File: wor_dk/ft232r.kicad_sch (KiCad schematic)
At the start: 22 parts, among them J401 USB_C_Receptacle_USB2.0_16P, U401 FT232RL

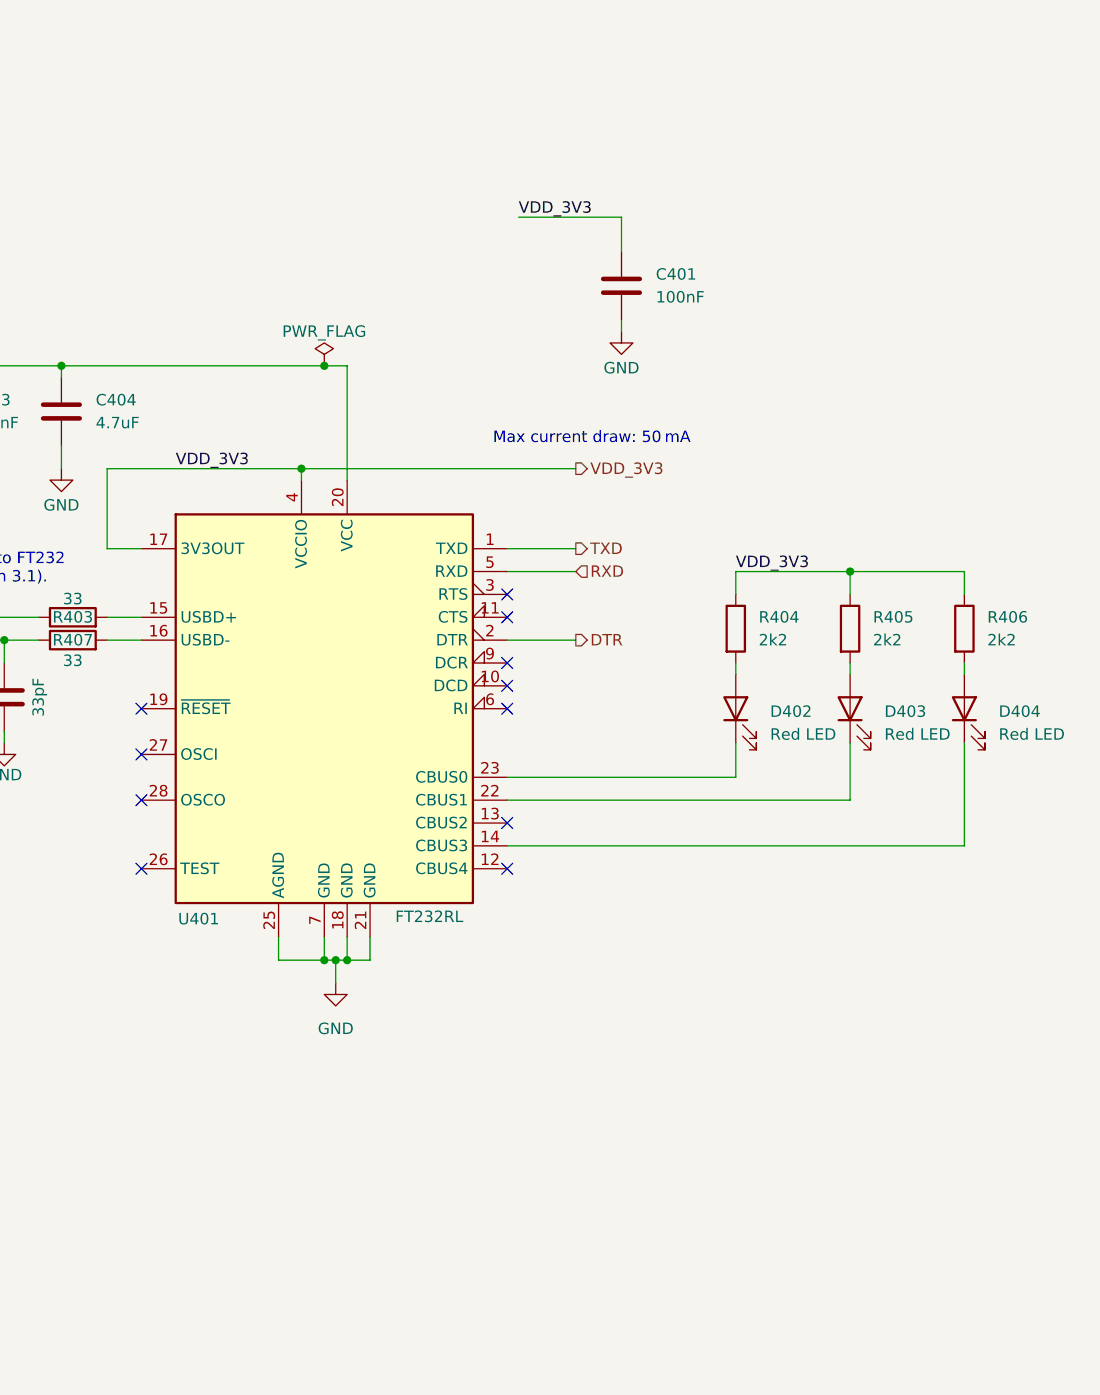
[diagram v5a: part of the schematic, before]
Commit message: wor_dk: add some comments to schematic
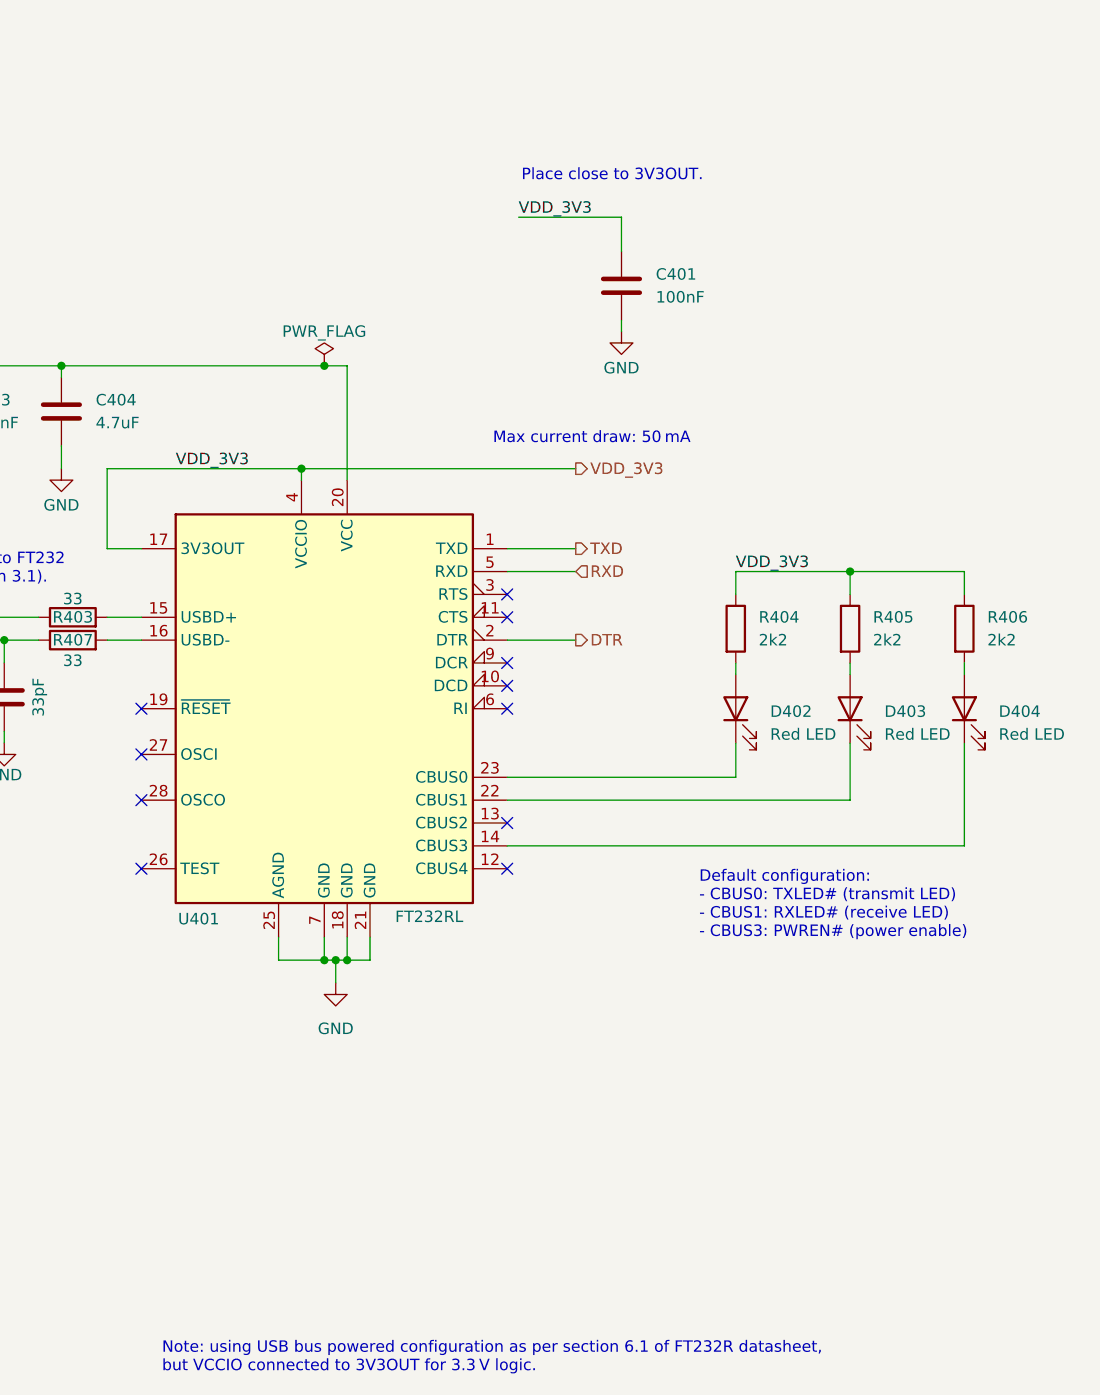
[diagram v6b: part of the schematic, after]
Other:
- note added: "Default configuration: - CBUS0: TXLED# (transmit LED) - CBUS1: RXLED# (receive LED) - CBUS3: PWREN# (power enable)"
- note added: "Note: using USB bus powered configuration as per section 6.1 of FT232R datasheet, but VCCIO connected to 3V3OUT for 3.3 V logic."
- note added: "Place close to 3V3OUT."
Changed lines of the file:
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@@
+		)
+	)
+	(text "Note: using USB bus powered configuration as per section 6.1 of FT232R datasheet,\nbut VCCIO connected to 3V3OUT for 3.3 V logic."
+		(exclude_from_sim no)
+		(at 178.816 171.196 0)
+		(effects
+			(font
+				(size 1.27 1.27)
+			)
+			(justify left)
 		)
 	)
@@
 		(effects
 			(font
+				(size 1.27 1.27)
+			)
+		)
+	)
+	(text "Default configuration:\n- CBUS0: TXLED# (transmit LED)\n- CBUS1: RXLED# (receive LED)\n- CBUS3: PWREN# (power enable)"
+		(exclude_from_sim no)
+		(at 238.506 120.904 0)
+		(effects
+			(font
+				(size 1.27 1.27)
+			)
+			(justify left)
+		)
+	)
+	(text "Place close to 3V3OUT."
+		(exclude_from_sim no)
+		(at 228.854 39.878 0)
+		(effects
+			(font

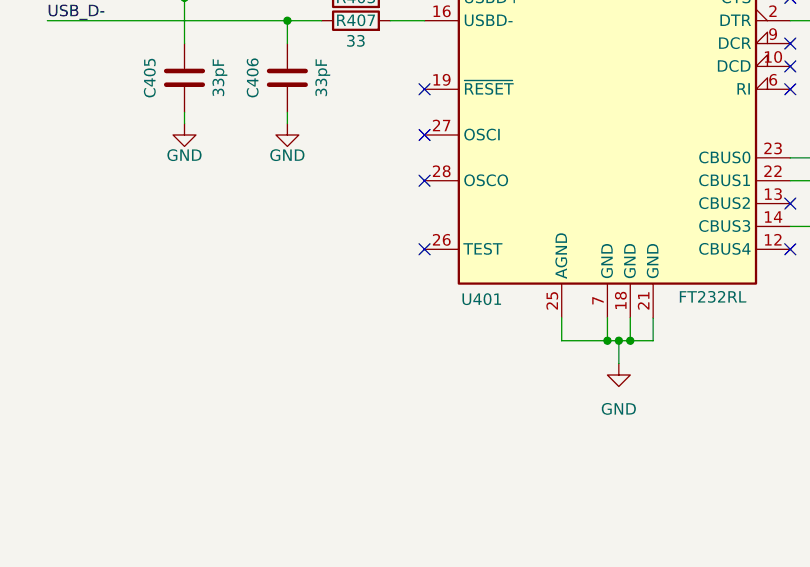
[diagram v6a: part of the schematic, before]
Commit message: wor_dk: schematic: FT232: fix: connect TEST to GND
The TEST pin must be connected to GND when not used; otherwise the
FT232 does not work properly.
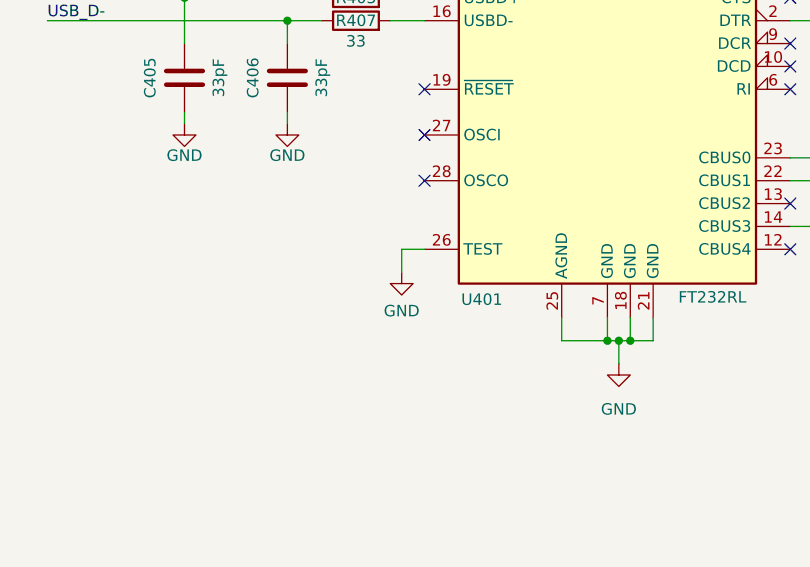
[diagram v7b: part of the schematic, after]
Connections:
- net GND: now also U401.26 (TEST)
- no-connect marks 13 -> 12
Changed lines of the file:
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@@
-	)
-	(no_connect
-		(at 176.53 116.84)
 	)
 	(no_connect
@@
 	(wire
 		(pts
+			(xy 173.99 119.38) (xy 173.99 116.84)
+		)
+		(stroke
+			(width 0)
+			(type default)
+		)
+	)
+	(wire
+		(pts
 			(xy 149.86 88.9) (xy 165.1 88.9)
 		)
@@
 		(pts
 			(xy 48.26 91.44) (xy 57.15 91.44)
+		)
+		(stroke
+			(width 0)
+			(type default)
+		)
+	)
+	(wire
+		(pts
+			(xy 173.99 116.84) (xy 176.53 116.84)
 		)
 		(stroke
@@
 					(unit 1)
 				)
+			)
+		)
+	)
+	(symbol
+		(lib_id "power:GND")
+		(at 173.99 119.38 0)
+		(unit 1)
+		(exclude_from_sim no)
+		(in_bom yes)
+		(on_board yes)
+		(dnp no)
+		(property "Reference" "#PWR0412"
+			(at 173.99 125.73 0)
+			(effects
+				(font
+					(size 1.27 1.27)
+				)
+				(hide yes)
+			)
+		)
+		(property "Value" "GND"
+			(at 173.99 123.698 0)
+			(effects
+				(font
+					(size 1.27 1.27)
+				)
+			)
+		)
+		(property "Footprint" ""
+			(at 173.99 119.38 0)
+			(effects
+				(font
+					(size 1.27 1.27)
+				)
+				(hide yes)
+			)
+		)
+		(property "Datasheet" ""
+			(at 173.99 119.38 0)
+			(effects
+				(font
+					(size 1.27 1.27)
+				)
+				(hide yes)
+			)
+		)
+		(property "Description" "Power symbol creates a global label with name \"GND\" , ground"
+			(at 173.99 119.38 0)
+			(effects
+				(font
+					(size 1.27 1.27)
+				)
+				(hide yes)
+			)
+		)
+		(pin "1"
+		)
+		(instances
+			(project ""
+				(path "/8d3147eb-060b-4f65-bf42-ed06a58b21ba/711499aa-b4ff-4669-a7c0-a5db1aab8120"
+					(reference "#PWR0412")
+					(unit 1)
+				)

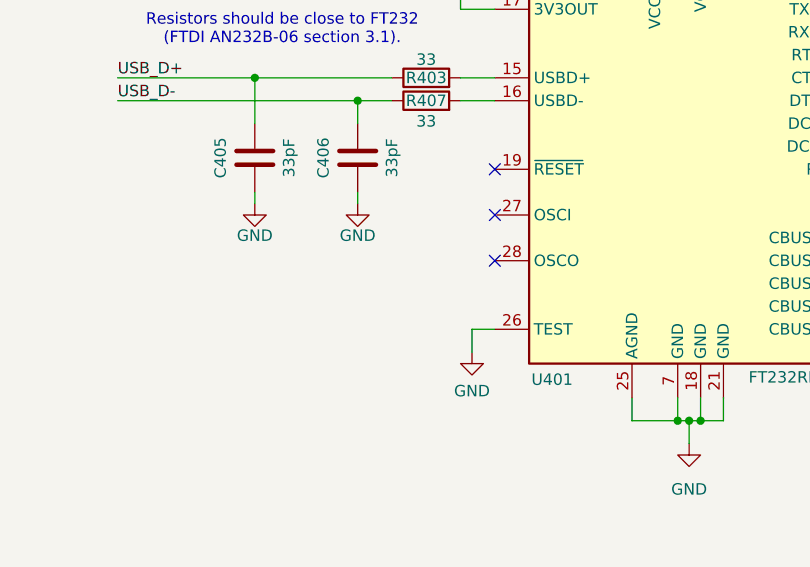
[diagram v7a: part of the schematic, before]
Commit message: wor_dk: schematic: add reset buttons for FT232 & LPC11U35
This is just for convenience.
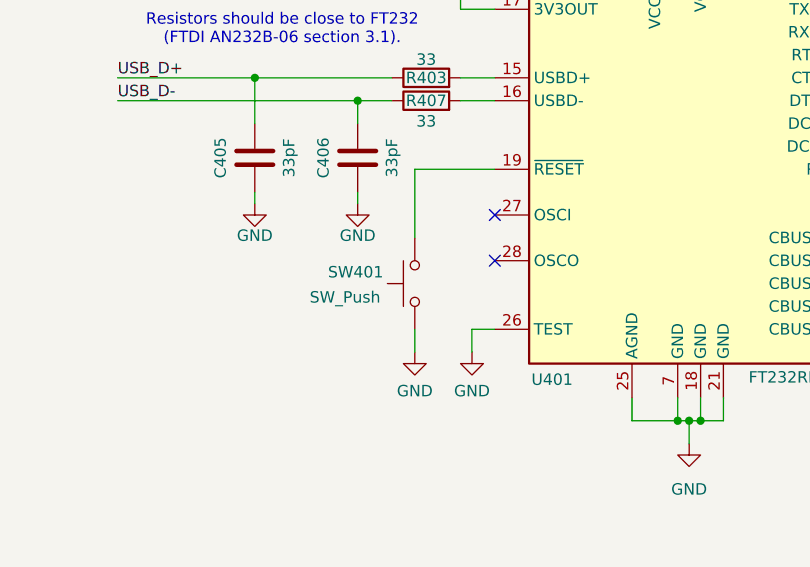
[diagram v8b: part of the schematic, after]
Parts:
- added SW401: SW_Push, Button_Switch_SMD:SW_SPST_PTS810, symbol Switch:SW_Push
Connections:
- net GND: now also SW401.1
- net at U401.19 (~{RESET}): now also SW401.2
- no-connect marks 12 -> 11
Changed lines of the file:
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@@
 	)
 	(no_connect
-		(at 176.53 99.06)
-	)
-	(no_connect
 		(at 217.17 111.76)
 	)
@@
 	(wire
 		(pts
+			(xy 167.64 99.06) (xy 167.64 106.68)
+		)
+		(stroke
+			(width 0)
+			(type default)
+		)
+	)
+	(wire
+		(pts
 			(xy 127 60.96) (xy 130.81 60.96)
 		)
@@
 	(wire
 		(pts
+			(xy 167.64 116.84) (xy 167.64 119.38)
+		)
+		(stroke
+			(width 0)
+			(type default)
+		)
+	)
+	(wire
+		(pts
 			(xy 201.93 124.46) (xy 201.93 127)
 		)
@@
 	(wire
 		(pts
+			(xy 176.53 99.06) (xy 167.64 99.06)
+		)
+		(stroke
+			(width 0)
+			(type default)
+		)
+	)
+	(wire
+		(pts
 			(xy 173.99 116.84) (xy 176.53 116.84)
 		)
@@
 	(symbol
 		(lib_id "power:GND")
+		(at 167.64 119.38 0)
+		(unit 1)
+		(exclude_from_sim no)
+		(in_bom yes)
+		(on_board yes)
+		(dnp no)
+		(property "Reference" "#PWR0413"
+			(at 167.64 125.73 0)
+			(effects
+				(font
+					(size 1.27 1.27)
+				)
+				(hide yes)
+			)
+		)
+		(property "Value" "GND"
+			(at 167.64 123.698 0)
+			(effects
+				(font
+					(size 1.27 1.27)
+				)
+			)
+		)
+		(property "Footprint" ""
+			(at 167.64 119.38 0)
+			(effects
+				(font
+					(size 1.27 1.27)
+				)
+				(hide yes)
+			)
+		)
+		(property "Datasheet" ""
+			(at 167.64 119.38 0)
+			(effects
+				(font
+					(size 1.27 1.27)
+				)
+				(hide yes)
+			)
+		)
+		(property "Description" "Power symbol creates a global label with name \"GND\" , ground"
+			(at 167.64 119.38 0)
+			(effects
+				(font
+					(size 1.27 1.27)
+				)
+				(hide yes)
+			)
+		)
+		(pin "1"
+		)
+		(instances
+			(project ""
+				(path "/8d3147eb-060b-4f65-bf42-ed06a58b21ba/711499aa-b4ff-4669-a7c0-a5db1aab8120"
+					(reference "#PWR0413")
+					(unit 1)
+				)
+			)
+		)
+	)
+	(symbol
+		(lib_id "power:GND")
 		(at 173.99 119.38 0)
 		(unit 1)
@@
 					(unit 1)
 				)
+			)
+		)
+	)
+	(symbol
+		(lib_id "Switch:SW_Push")
+		(at 167.64 111.76 90)
+		(unit 1)
+		(exclude_from_sim no)
+		(in_bom yes)
+		(on_board yes)
+		(dnp no)
+		(property "Reference" "SW401"
+			(at 157.988 110.49 90)
+			(effects
+				(font
+					(size 1.27 1.27)
+				)
+				(justify right)
+			)
+		)
+		(property "Value" "SW_Push"
+			(at 155.956 113.284 90)
+			(effects
+				(font
+					(size 1.27 1.27)
+				)
+				(justify right)
+			)
+		)
+		(property "Footprint" "Button_Switch_SMD:SW_SPST_PTS810"
+			(at 162.56 111.76 0)
+			(effects
+				(font
+					(size 1.27 1.27)
+				)
+				(hide yes)
+			)
+		)
+		(property "Datasheet" "https://www.ckswitches.com/media/1476/pts810.pdf"
+			(at 162.56 111.76 0)
+			(effects
+				(font
+					(size 1.27 1.27)
+				)
+				(hide yes)
+			)
+		)
+		(property "Description" ""
+			(at 167.64 111.76 0)
+			(effects
+				(font
+					(size 1.27 1.27)
+				)
+				(hide yes)
+			)
+		)
+		(property "Manufacturer" "C&K"
+			(at 167.64 111.76 0)
+			(effects
+				(font
+					(size 1.27 1.27)
+				)
+				(hide yes)
+			)
+		)
+		(property "Part Number" "PTS810 SJK 250 SMTR LFS"
+			(at 167.64 111.76 0)
+			(effects
+				(font
+					(size 1.27 1.27)
+				)
+				(hide yes)
+			)
+		)
+		(property "LCSC" "C221896"
+			(at 167.64 111.76 0)
+			(effects
+				(font
+					(size 1.27 1.27)
+				)
+				(hide yes)
+			)
+		)
+		(pin "1"
+		)
+		(pin "2"
+		)
+		(instances
+			(project "wor_dk"
+				(path "/8d3147eb-060b-4f65-bf42-ed06a58b21ba/711499aa-b4ff-4669-a7c0-a5db1aab8120"
+					(reference "SW401")
+					(unit 1)
+				)
